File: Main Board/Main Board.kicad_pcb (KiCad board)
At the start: 2 copper layers, 69.9 x 49.5 mm, 12 parts, among them J1 Conn_01x02, J2 Conn_02x05_Odd_Even, J3 Conn_01x06, J4 Conn_01x06, J5 Conn_01x02, J6 Conn_01x02

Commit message: Update connectors and layout
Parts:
- removed J5, J6: Conn_01x02, Connector_JST:JST_EH_B2B-EH-A_1x02_P2.50mm_Vertical
- J1: value Conn_01x02 -> Conn_01x05; footprint Connector_JST:JST_EH_B2B-EH-A_1x02_P2.50mm_Vertical -> Connector_JST:JST_XH_B5B-XH-A_1x05_P2.50mm_Vertical
- J2: value Conn_02x05_Odd_Even -> Conn_01x05; footprint Connector_PinHeader_2.54mm:PinHeader_2x05_P2.54mm_Vertical -> Connector_JST:JST_XH_B5B-XH-A_1x05_P2.50mm_Vertical
- J3, J4: value Conn_01x06 -> Conn_01x04; footprint Connector_PinHeader_2.54mm:PinHeader_1x06_P2.54mm_Vertical -> Connector_JST:JST_XH_B4B-XH-A_1x04_P2.50mm_Vertical
- moved J1 46.2 mm to (120.7, 100.5), turned to 270 degrees
- moved J4 28.8 mm to (132.1, 123.3), turned to 270 degrees
- moved J3 23.7 mm to (132.1, 95.2), turned to 270 degrees
- moved J2 14.5 mm to (120.7, 116.8), turned to 270 degrees
- moved REF** 14.0 mm to (119.4, 94.0)
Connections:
- A1 pad 10: /R_IN_1 -> /M2_IN_1
- A1 pad 11: /R_IN_2 -> /M2_IN_2
- A1 pad 12: /R_Enable -> /M2_Enable
- A1 pad 14: /R_Encoder_B -> /M2_Encoder_B
- A1 pad 15: /L_Encoder_B -> /M1_Encoder_B
- A1 pad 5: /L_Encoder_A -> /M1_Encoder_A
- A1 pad 6: /R_Encoder_A -> /M2_Encoder_A
- A1 pad 7: /L_IN_1 -> /M1_IN_1
- A1 pad 8: /L_IN_2 -> /M1_IN_2
- A1 pad 9: /L_Enable -> /M1_Enable
- J1 pad 1: GND -> +5V
- J1 pad 2: +5V -> /M1_Enable
- J2 pad 2: +5V -> /M2_Enable
- J2 pad 3: /L_Enable -> /M2_IN_1
- J2 pad 4: /R_Enable -> /M2_IN_2
- J2 pad 5: /L_IN_1 -> GND
- J3 pad 1: /L_Motor_- -> GND
- J3 pad 2: /L_Motor_+ -> +5V
- J3 pad 3: GND -> /M1_Encoder_A
- J3 pad 4: +5V -> /M1_Encoder_B
- J4 pad 1: /R_Motor_- -> GND
- J4 pad 2: /R_Motor_+ -> +5V
- J4 pad 3: GND -> /M2_Encoder_A
- J4 pad 4: +5V -> /M2_Encoder_B
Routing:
- net /L_Encoder_A: track 42.1 -> 0.00 mm
- net /M2_Encoder_A: track 0.00 -> 41.8 mm
- net /R_Encoder_B: track 38.5 -> 0.00 mm
- net /M1_Encoder_B: track 0.00 -> 32.5 mm
- net /M1_Enable: track 0.00 -> 31.9 mm
- net /M2_Enable: track 0.00 -> 28.7 mm
- net /M1_IN_2: track 0.00 -> 22.4 mm
- net /M1_IN_1: track 0.00 -> 22.4 mm
- net /M2_IN_1: track 0.00 -> 21.9 mm
- net /M2_IN_2: track 0.00 -> 21.8 mm
- net /R_Enable: track 18.1 -> 0.00 mm
- net /L_Enable: track 17.0 -> 0.00 mm
- net /R_Encoder_A: track 16.3 -> 0.00 mm
- net /L_Encoder_B: track 15.2 -> 0.00 mm
- net /M1_Encoder_A: track 0.00 -> 11.0 mm
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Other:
- board text added: "Motor 1"
- board text added: "Motor 2"
- board text added: "SCR NRC 2020 Main Board"

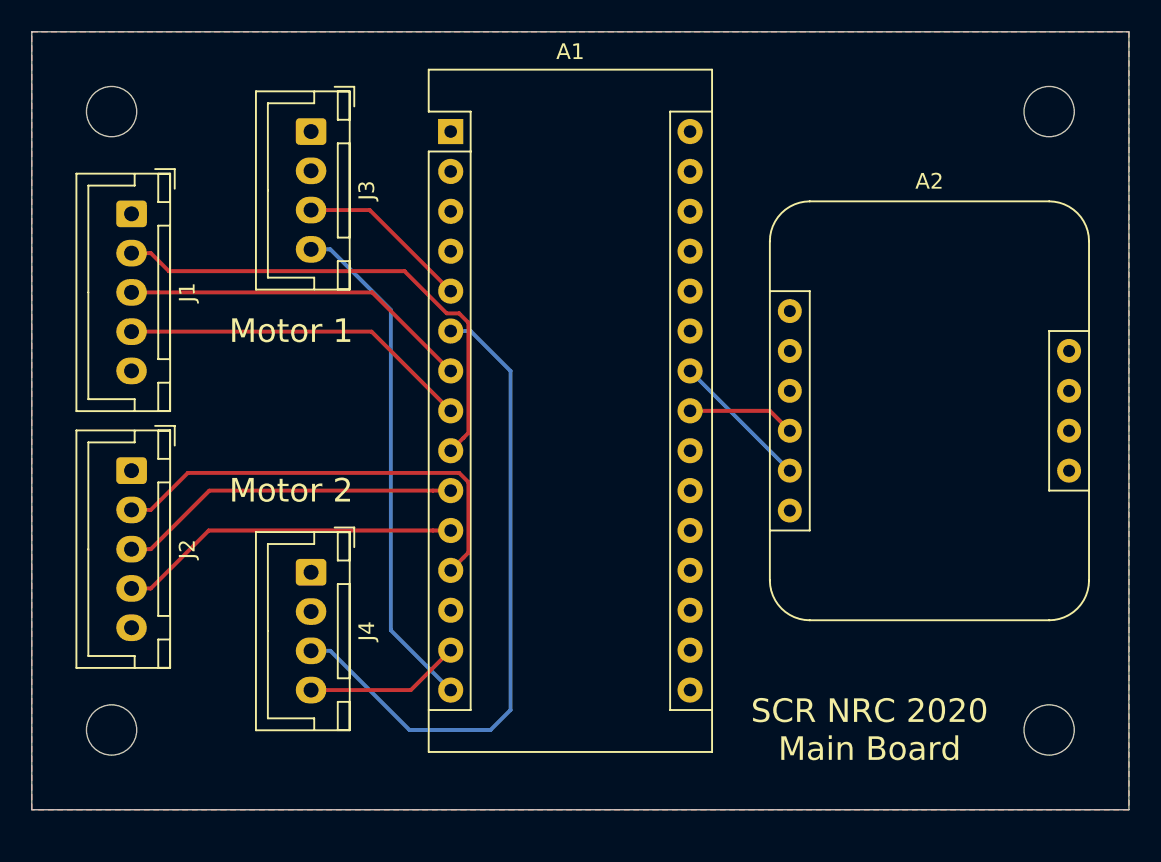
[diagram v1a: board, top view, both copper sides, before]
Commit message: Adjust component spacing
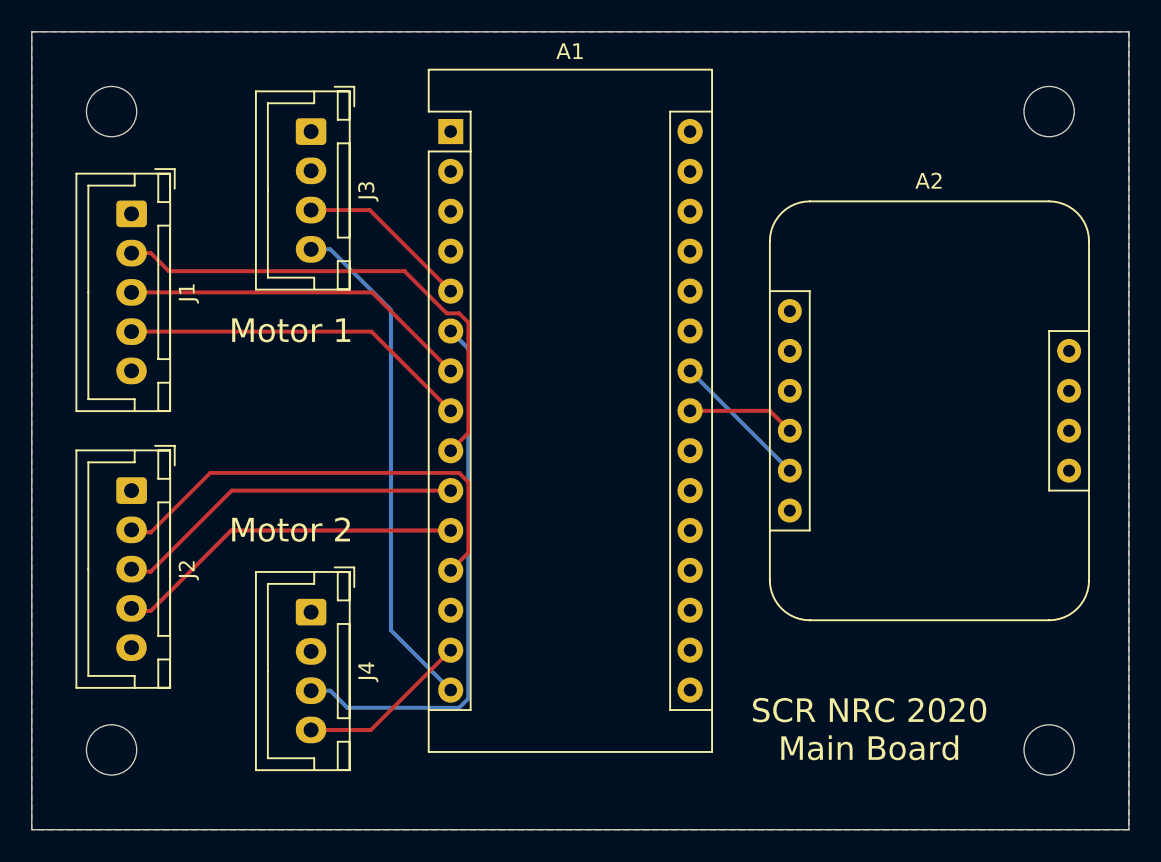
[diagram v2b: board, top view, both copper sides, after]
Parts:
- moved J4 2.54 mm to (132.1, 125.8)
- moved REF** 1.27 mm to (119.4, 134.6)
- moved REF** 1.27 mm to (179.1, 134.6)
- moved J2 1.27 mm to (120.7, 118.1)
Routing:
- net /M2_Encoder_A: track 41.8 -> 34.6 mm
- net /M2_Encoder_B: track 9.94 -> 11.0 mm
- net /M2_IN_1: track 21.9 -> 22.5 mm
- net /M2_Enable: track 28.7 -> 29.3 mm
- net /M2_IN_2: track 21.8 -> 22.4 mm
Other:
- board size 69.9 x 49.5 mm -> 69.9 x 50.8 mm
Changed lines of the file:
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@@
     (thickness 1.6)
     (drawings 7)
-    (tracks 46)
+    (tracks 41)
     (zones 0)
     (modules 10)
@@
   )
   (module Connector_JST:JST_XH_B4B-XH-A_1x04_P2.50mm_Vertical (layer F.Cu)
-    (at 132.08 123.31 270)
+    (at 132.08 125.85 270)
     (descr "JST XH series connector, B4B-XH-A (http://www.jst-mfg.com/product/pdf/eng/eXH.pdf), generated with kicad-footprint-generator")
     (tags "connector JST XH vertical")
@@
   )
   (module Connector_JST:JST_XH_B5B-XH-A_1x05_P2.50mm_Vertical (layer F.Cu)
-    (at 120.65 116.84 270)
+    (at 120.65 118.11 270)
     (descr "JST XH series connector, B5B-XH-A (http://www.jst-mfg.com/product/pdf/eng/eXH.pdf), generated with kicad-footprint-generator")
     (tags "connector JST XH vertical")
@@
   )
   (module MountingHole:MountingHole_3.2mm_M3 (layer F.Cu)
-    (at 119.38 133.35)
+    (at 119.38 134.62)
     (descr "Mounting Hole 3.2mm, no annular, M3")
     (tags "mounting hole 3.2mm no annular m3")
@@
   )
   (module MountingHole:MountingHole_3.2mm_M3 (layer F.Cu)
-    (at 179.07 133.35)
+    (at 179.07 134.62)
     (descr "Mounting Hole 3.2mm, no annular, M3")
     (tags "mounting hole 3.2mm no annular m3")
@@
     (effects (font (size 1.5 1.5) (thickness 0.3)))
   )
-  (gr_text "Motor 2" (at 130.81 118.11) (layer F.SilkS)
+  (gr_text "Motor 2" (at 130.81 120.65) (layer F.SilkS)
     (effects (font (size 1.5 1.5) (thickness 0.3)))
   )
@@
     (effects (font (size 1.5 1.5) (thickness 0.3)))
   )
-  (gr_line (start 114.3 138.43) (end 114.3 88.9) (layer Edge.Cuts) (width 0.05))
-  (gr_line (start 184.15 138.43) (end 114.3 138.43) (layer Edge.Cuts) (width 0.05))
-  (gr_line (start 184.15 88.9) (end 184.15 138.43) (layer Edge.Cuts) (width 0.05))
+  (gr_line (start 114.3 139.7) (end 114.3 88.9) (layer Edge.Cuts) (width 0.05))
+  (gr_line (start 184.15 139.7) (end 114.3 139.7) (layer Edge.Cuts) (width 0.05))
+  (gr_line (start 184.15 88.9) (end 184.15 139.7) (layer Edge.Cuts) (width 0.05))
   (gr_line (start 114.3 88.9) (end 184.15 88.9) (layer Edge.Cuts) (width 0.05))
   (segment (start 156.21 110.49) (end 162.56 116.84) (width 0.25) (layer B.Cu) (net 9) (status 30))
@@
   (segment (start 156.21 113.03) (end 161.29 113.03) (width 0.25) (layer F.Cu) (net 10) (status 10))
   (segment (start 133.305 102.75) (end 137.16 106.605) (width 0.25) (layer B.Cu) (net 26))
-  (segment (start 132.08 102.75) (end 133.305 102.75) (width 0.25) (layer B.Cu) (net 26))
-  (segment (start 137.16 127) (end 140.97 130.81) (width 0.25) (layer B.Cu) (net 26))
+  (segment (start 132.08 102.75) (end 133.305 102.75) (width 0.25) (layer B.Cu) (net 26) (status 10))
+  (segment (start 137.16 127) (end 140.97 130.81) (width 0.25) (layer B.Cu) (net 26) (status 20))
   (segment (start 137.16 106.605) (end 137.16 127) (width 0.25) (layer B.Cu) (net 26))
-  (segment (start 138.43 130.81) (end 140.97 128.27) (width 0.25) (layer F.Cu) (net 27))
-  (segment (start 132.08 130.81) (end 138.43 130.81) (width 0.25) (layer F.Cu) (net 27))
-  (segment (start 141.769999 122.390001) (end 140.97 123.19) (width 0.25) (layer F.Cu) (net 28))
-  (segment (start 142.095001 122.064999) (end 141.769999 122.390001) (width 0.25) (layer F.Cu) (net 28))
+  (segment (start 135.89 133.35) (end 140.97 128.27) (width 0.25) (layer F.Cu) (net 27) (status 20))
+  (segment (start 132.08 133.35) (end 135.89 133.35) (width 0.25) (layer F.Cu) (net 27) (status 10))
+  (segment (start 142.095001 122.064999) (end 140.97 123.19) (width 0.25) (layer F.Cu) (net 28) (status 20))
   (segment (start 142.095001 117.569999) (end 142.095001 122.064999) (width 0.25) (layer F.Cu) (net 28))
   (segment (start 141.510001 116.984999) (end 142.095001 117.569999) (width 0.25) (layer F.Cu) (net 28))
-  (segment (start 124.230001 116.984999) (end 141.510001 116.984999) (width 0.25) (layer F.Cu) (net 28))
-  (segment (start 121.875 119.34) (end 124.230001 116.984999) (width 0.25) (layer F.Cu) (net 28))
-  (segment (start 120.65 119.34) (end 121.875 119.34) (width 0.25) (layer F.Cu) (net 28))
-  (segment (start 139.83863 120.65) (end 140.97 120.65) (width 0.25) (layer F.Cu) (net 29))
-  (segment (start 125.565 120.65) (end 139.83863 120.65) (width 0.25) (layer F.Cu) (net 29))
-  (segment (start 121.875 124.34) (end 125.565 120.65) (width 0.25) (layer F.Cu) (net 29))
-  (segment (start 120.65 124.34) (end 121.875 124.34) (width 0.25) (layer F.Cu) (net 29))
-  (segment (start 125.605 118.11) (end 139.83863 118.11) (width 0.25) (layer F.Cu) (net 30))
-  (segment (start 139.83863 118.11) (end 140.97 118.11) (width 0.25) (layer F.Cu) (net 30))
-  (segment (start 121.875 121.84) (end 125.605 118.11) (width 0.25) (layer F.Cu) (net 30))
-  (segment (start 120.65 121.84) (end 121.875 121.84) (width 0.25) (layer F.Cu) (net 30))
+  (segment (start 125.660001 116.984999) (end 141.510001 116.984999) (width 0.25) (layer F.Cu) (net 28))
+  (segment (start 121.875 120.77) (end 125.660001 116.984999) (width 0.25) (layer F.Cu) (net 28))
+  (segment (start 120.65 120.77) (end 121.875 120.77) (width 0.25) (layer F.Cu) (net 28) (status 10))
+  (segment (start 126.995 120.65) (end 140.97 120.65) (width 0.25) (layer F.Cu) (net 29) (status 20))
+  (segment (start 121.875 125.77) (end 126.995 120.65) (width 0.25) (layer F.Cu) (net 29))
+  (segment (start 120.65 125.77) (end 121.875 125.77) (width 0.25) (layer F.Cu) (net 29) (status 10))
+  (segment (start 127.035 118.11) (end 140.97 118.11) (width 0.25) (layer F.Cu) (net 30) (status 20))
+  (segment (start 121.875 123.27) (end 127.035 118.11) (width 0.25) (layer F.Cu) (net 30))
+  (segment (start 120.65 123.27) (end 121.875 123.27) (width 0.25) (layer F.Cu) (net 30) (status 10))
   (segment (start 141.510001 106.824999) (end 142.095001 107.409999) (width 0.25) (layer F.Cu) (net 31))
-  (segment (start 141.769999 114.770001) (end 140.97 115.57) (width 0.25) (layer F.Cu) (net 31))
+  (segment (start 142.095001 114.444999) (end 140.97 115.57) (width 0.25) (layer F.Cu) (net 31) (status 20))
   (segment (start 142.095001 107.409999) (end 142.095001 114.444999) (width 0.25) (layer F.Cu) (net 31))
   (segment (start 140.719997 106.824999) (end 141.510001 106.824999) (width 0.25) (layer F.Cu) (net 31))
@@
   (segment (start 123.025 104.14) (end 138.034998 104.14) (width 0.25) (layer F.Cu) (net 31))
   (segment (start 121.875 102.99) (end 123.025 104.14) (width 0.25) (layer F.Cu) (net 31))
-  (segment (start 142.095001 114.444999) (end 141.769999 114.770001) (width 0.25) (layer F.Cu) (net 31))
-  (segment (start 120.65 102.99) (end 121.875 102.99) (width 0.25) (layer F.Cu) (net 31))
-  (segment (start 135.93 107.99) (end 140.97 113.03) (width 0.25) (layer F.Cu) (net 32))
-  (segment (start 120.65 107.99) (end 135.93 107.99) (width 0.25) (layer F.Cu) (net 32))
-  (segment (start 135.97 105.49) (end 140.97 110.49) (width 0.25) (layer F.Cu) (net 33))
-  (segment (start 120.65 105.49) (end 135.97 105.49) (width 0.25) (layer F.Cu) (net 33))
-  (segment (start 142.24 107.95) (end 140.97 107.95) (width 0.25) (layer B.Cu) (net 34))
-  (segment (start 144.78 110.49) (end 142.24 107.95) (width 0.25) (layer B.Cu) (net 34))
-  (segment (start 132.08 128.31) (end 133.305 128.31) (width 0.25) (layer B.Cu) (net 34))
-  (segment (start 138.345 133.35) (end 143.51 133.35) (width 0.25) (layer B.Cu) (net 34))
-  (segment (start 133.305 128.31) (end 138.345 133.35) (width 0.25) (layer B.Cu) (net 34))
-  (segment (start 143.51 133.35) (end 144.78 132.08) (width 0.25) (layer B.Cu) (net 34))
-  (segment (start 144.78 132.08) (end 144.78 110.49) (width 0.25) (layer B.Cu) (net 34))
-  (segment (start 135.81 100.25) (end 140.97 105.41) (width 0.25) (layer F.Cu) (net 35))
-  (segment (start 132.08 100.25) (end 135.81 100.25) (width 0.25) (layer F.Cu) (net 35))
+  (segment (start 120.65 102.99) (end 121.875 102.99) (width 0.25) (layer F.Cu) (net 31) (status 10))
+  (segment (start 135.93 107.99) (end 140.97 113.03) (width 0.25) (layer F.Cu) (net 32) (status 20))
+  (segment (start 120.65 107.99) (end 135.93 107.99) (width 0.25) (layer F.Cu) (net 32) (status 10))
+  (segment (start 135.97 105.49) (end 140.97 110.49) (width 0.25) (layer F.Cu) (net 33) (status 20))
+  (segment (start 120.65 105.49) (end 135.97 105.49) (width 0.25) (layer F.Cu) (net 33) (status 10))
+  (segment (start 142.095001 109.075001) (end 140.97 107.95) (width 0.25) (layer B.Cu) (net 34) (status 20))
+  (segment (start 142.095001 131.350001) (end 142.095001 109.075001) (width 0.25) (layer B.Cu) (net 34))
+  (segment (start 141.510001 131.935001) (end 142.095001 131.350001) (width 0.25) (layer B.Cu) (net 34))
+  (segment (start 133.305 130.85) (end 134.390001 131.935001) (width 0.25) (layer B.Cu) (net 34))
+  (segment (start 134.390001 131.935001) (end 141.510001 131.935001) (width 0.25) (layer B.Cu) (net 34))
+  (segment (start 132.08 130.85) (end 133.305 130.85) (width 0.25) (layer B.Cu) (net 34) (status 10))
+  (segment (start 135.81 100.25) (end 140.97 105.41) (width 0.25) (layer F.Cu) (net 35) (status 20))
+  (segment (start 132.08 100.25) (end 135.81 100.25) (width 0.25) (layer F.Cu) (net 35) (status 10))
   (zone (net 3) (net_name GND) (layer B.Cu) (hatch edge 0.508)
     (connect_pads (clearance 0.508))
@@
     (polygon
       (pts
-        (xy 184.15 138.43) (xy 114.3 138.43) (xy 114.3 88.9) (xy 184.15 88.9)
+        (xy 184.15 139.7) (xy 114.3 139.7) (xy 114.3 88.9) (xy 184.15 88.9)
       )
     )
@@
     (polygon
       (pts
-        (xy 184.15 138.43) (xy 114.3 138.43) (xy 114.3 88.9) (xy 184.15 88.9)
+        (xy 184.15 139.7) (xy 114.3 139.7) (xy 114.3 88.9) (xy 184.15 88.9)
       )
     )

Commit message: Add logos to board
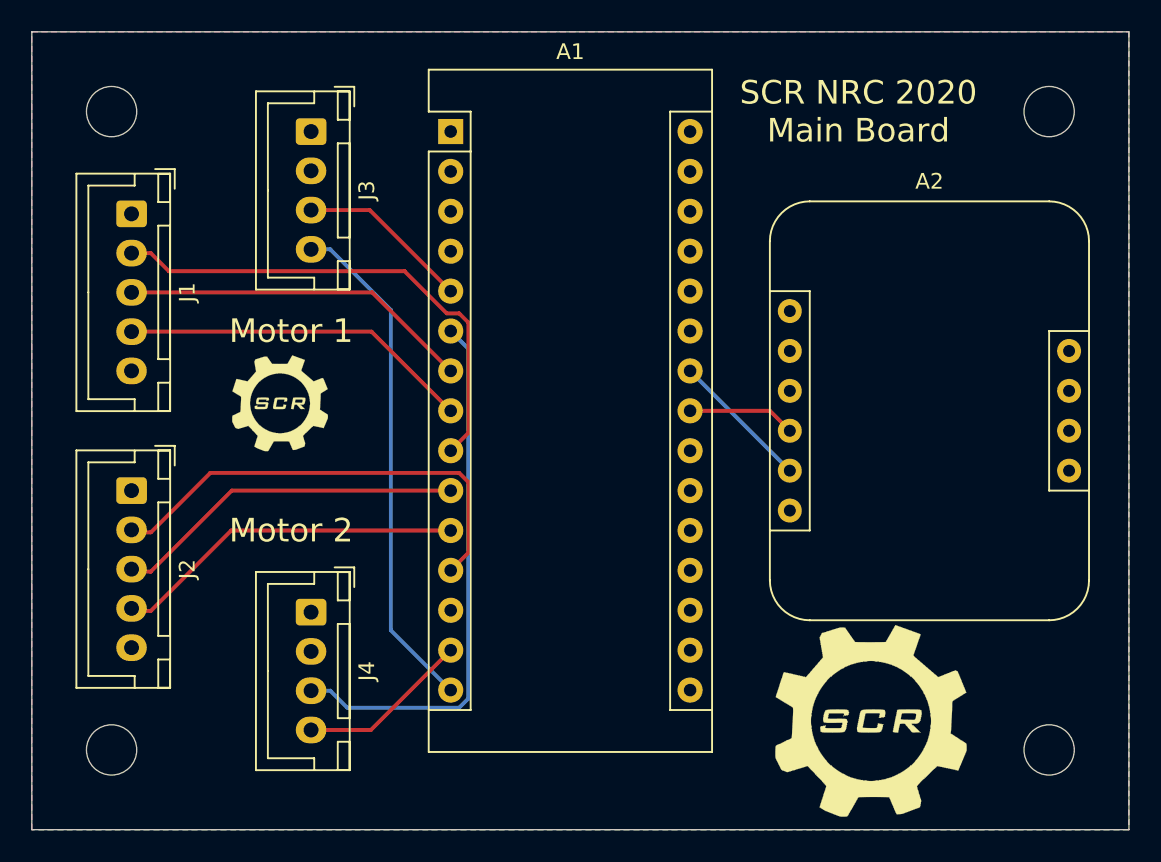
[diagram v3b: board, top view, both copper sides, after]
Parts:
- added G***: LOGO, SCR_KiCAD_Lib:scr-logo, B.Cu at (170.4, 99.6)
- added G***: LOGO, SCR_KiCAD_Lib:small-scr-logo, F.Cu at (130.1, 112.5)
- added G***: LOGO, SCR_KiCAD_Lib:scr-logo, F.Cu at (167.7, 132.8)
